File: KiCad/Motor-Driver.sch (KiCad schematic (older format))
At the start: 38 parts

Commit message: controller board schematic complete
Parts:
- gave numbers to parts that had none: 38

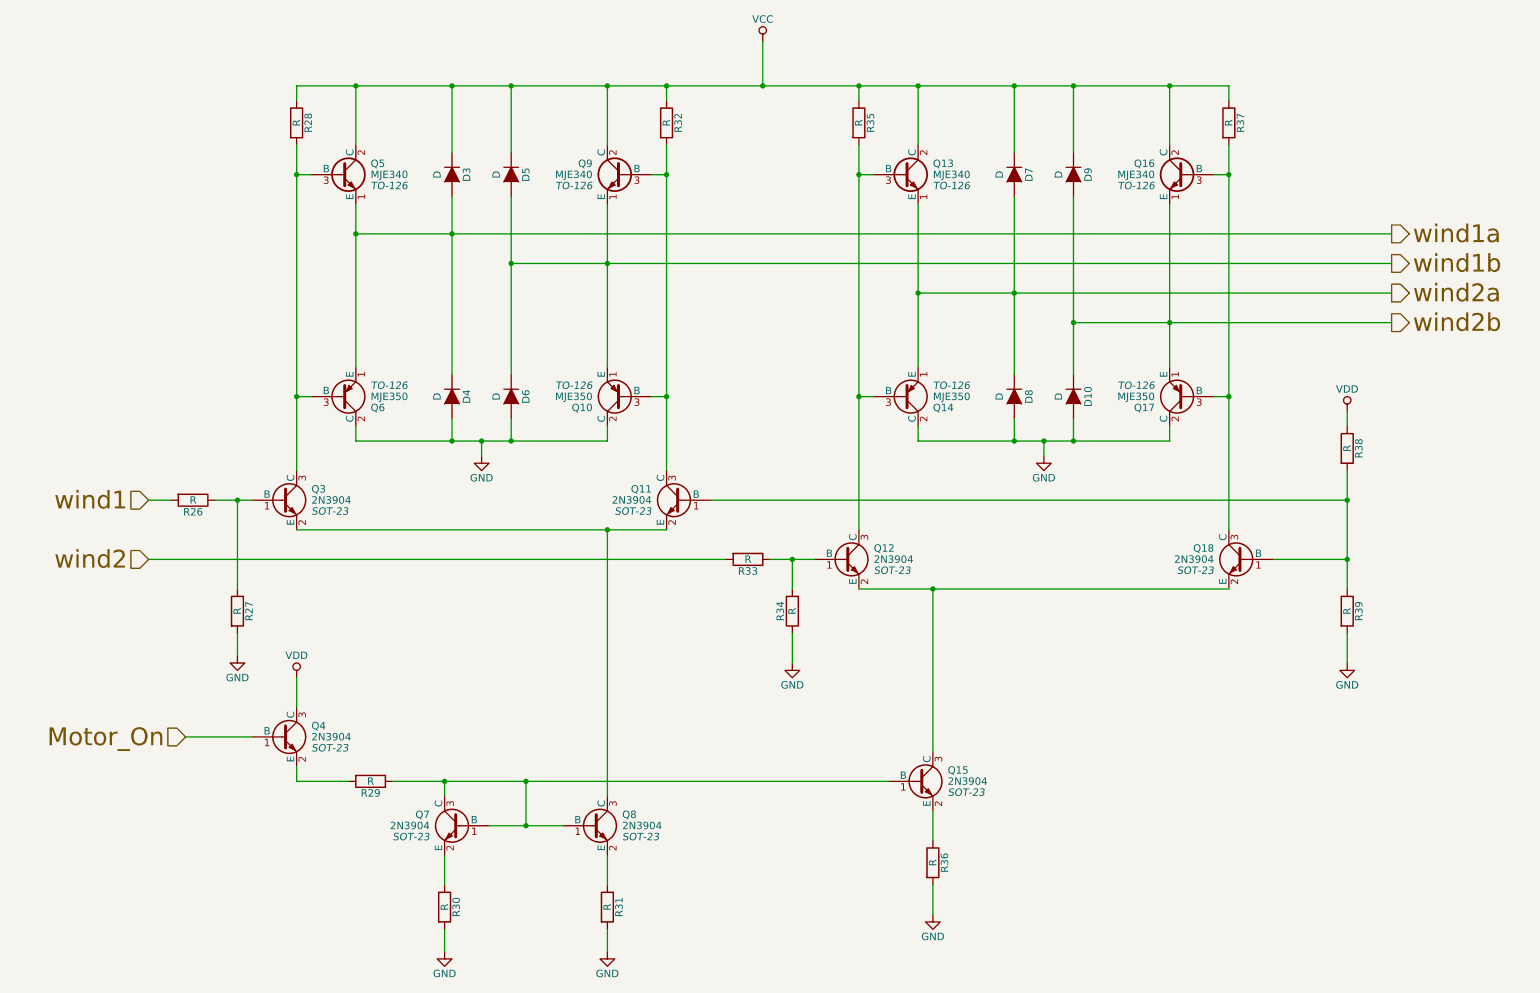
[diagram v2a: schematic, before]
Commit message: HeatOn fix, replaced R1-8 with array
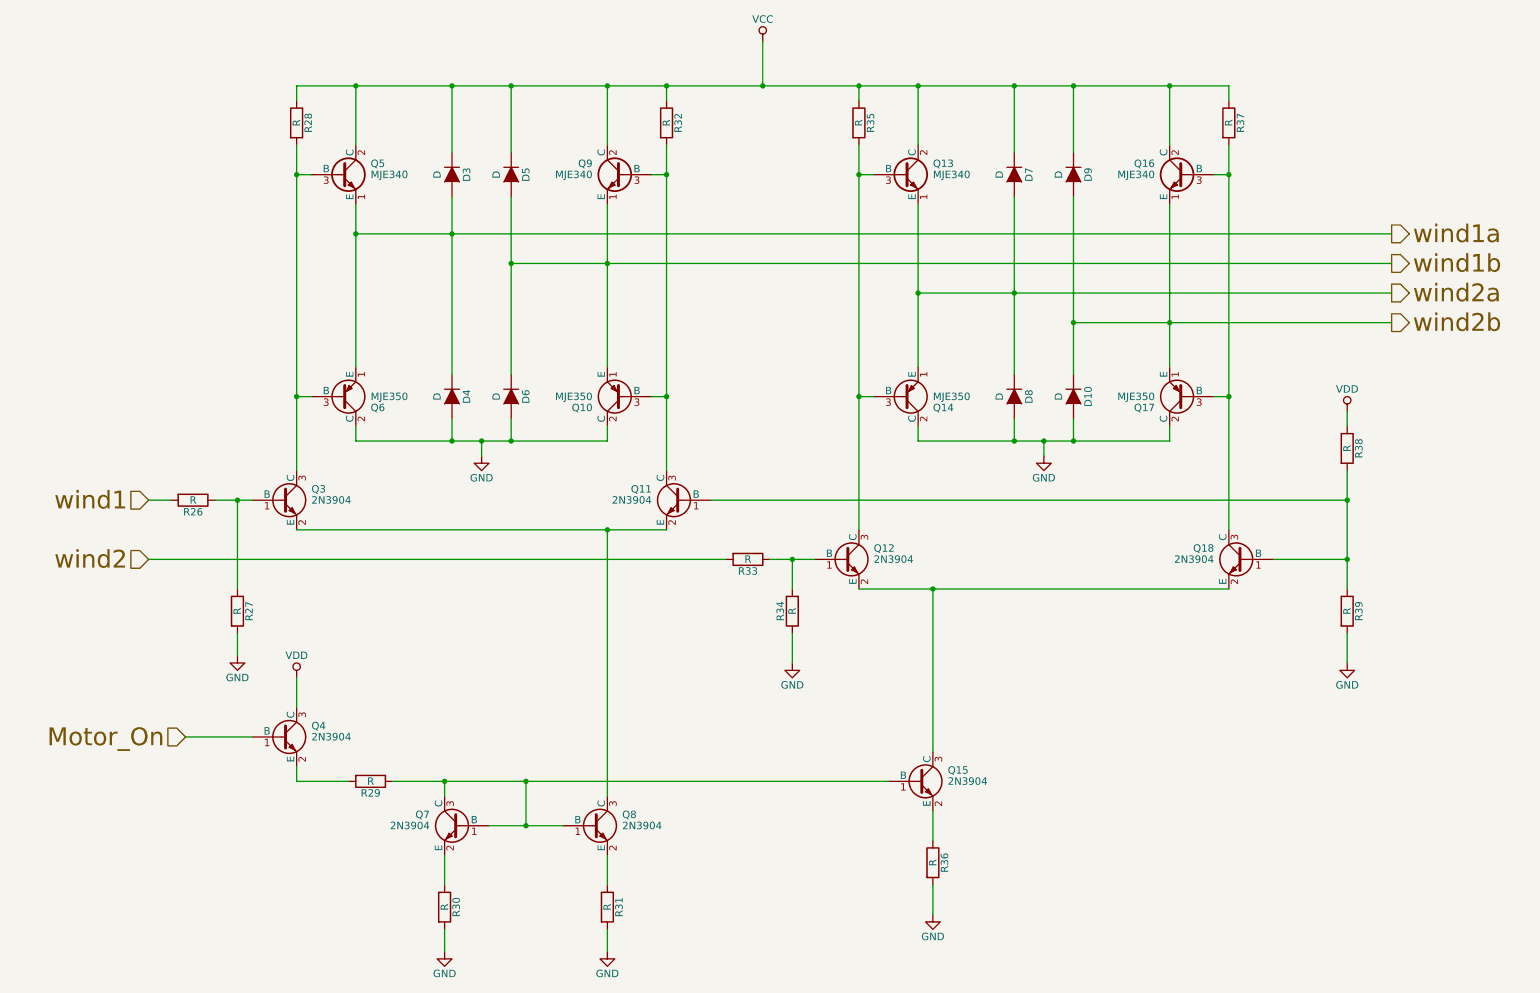
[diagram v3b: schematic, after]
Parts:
- Q10, Q13, Q14, Q16, Q17, Q5, Q6, Q9: footprint TO-126 -> (none)
- Q11, Q12, Q15, Q18, Q3, Q4, Q7, Q8: footprint SOT-23 -> (none)

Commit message: motor driver design
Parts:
- R26: value R -> 140
- R27: value R -> 115
- R28: renamed from R33; value R -> 140
- R29: renamed from R34; value R -> 115
- R30: renamed from R38; value R -> 64
- R31: renamed from R39; value R -> 64
- R32: renamed from R28; value R -> 165
- R33: renamed from R32; value R -> 165
- R34: renamed from R35; value R -> 165
- R35: renamed from R37; value R -> 165
- R36: renamed from R29; value R -> 51
- R37: renamed from R30; value R -> 10
- R38: renamed from R31; value R -> 10
- R39: renamed from R36; value R -> 10
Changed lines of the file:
@@
 $Descr A4 11693 8268
 encoding utf-8
-Sheet 4 6
+Sheet 5 6
 Title ""
 Date ""
@@
 $EndComp
 $Comp
-L R R28
+L R R32
 U 1 1 5681F689
 P 2300 1750
-F 0 "R28" V 2380 1750 50  0000 C CNN
-F 1 "R" V 2300 1750 50  0000 C CNN
+F 0 "R32" V 2380 1750 50  0000 C CNN
+F 1 "165" V 2300 1750 50  0000 C CNN
 F 2 "" V 2230 1750 50  0001 C CNN
 F 3 "" H 2300 1750 50  0000 C CNN
@@
 $EndComp
 $Comp
-L R R32
+L R R33
 U 1 1 5681F6D4
 P 4800 1750
-F 0 "R32" V 4880 1750 50  0000 C CNN
-F 1 "R" V 4800 1750 50  0000 C CNN
+F 0 "R33" V 4880 1750 50  0000 C CNN
+F 1 "165" V 4800 1750 50  0000 C CNN
 F 2 "" V 4730 1750 50  0001 C CNN
 F 3 "" H 4800 1750 50  0000 C CNN
@@
 $EndComp
 $Comp
-L R R35
+L R R34
 U 1 1 5681F715
 P 6100 1750
-F 0 "R35" V 6180 1750 50  0000 C CNN
-F 1 "R" V 6100 1750 50  0000 C CNN
+F 0 "R34" V 6180 1750 50  0000 C CNN
+F 1 "165" V 6100 1750 50  0000 C CNN
 F 2 "" V 6030 1750 50  0001 C CNN
 F 3 "" H 6100 1750 50  0000 C CNN
@@
 $EndComp
 $Comp
-L R R37
+L R R35
 U 1 1 5681F758
 P 8600 1750
-F 0 "R37" V 8680 1750 50  0000 C CNN
-F 1 "R" V 8600 1750 50  0000 C CNN
+F 0 "R35" V 8680 1750 50  0000 C CNN
+F 1 "165" V 8600 1750 50  0000 C CNN
 F 2 "" V 8530 1750 50  0001 C CNN
 F 3 "" H 8600 1750 50  0000 C CNN
@@
 $EndComp
 $Comp
-L R R38
+L R R30
 U 1 1 5681FC40
 P 9400 3950
-F 0 "R38" V 9480 3950 50  0000 C CNN
-F 1 "R" V 9400 3950 50  0000 C CNN
+F 0 "R30" V 9480 3950 50  0000 C CNN
+F 1 "64" V 9400 3950 50  0000 C CNN
 F 2 "" V 9330 3950 50  0001 C CNN
 F 3 "" H 9400 3950 50  0000 C CNN
@@
 $EndComp
 $Comp
-L R R39
+L R R31
 U 1 1 5681FD0B
 P 9400 5050
-F 0 "R39" V 9480 5050 50  0000 C CNN
-F 1 "R" V 9400 5050 50  0000 C CNN
+F 0 "R31" V 9480 5050 50  0000 C CNN
+F 1 "64" V 9400 5050 50  0000 C CNN
 F 2 "" V 9330 5050 50  0001 C CNN
 F 3 "" H 9400 5050 50  0000 C CNN
@@
 P 1600 4300
 F 0 "R26" V 1680 4300 50  0000 C CNN
-F 1 "R" V 1600 4300 50  0000 C CNN
+F 1 "140" V 1600 4300 50  0000 C CNN
 F 2 "" V 1530 4300 50  0001 C CNN
 F 3 "" H 1600 4300 50  0000 C CNN
@@
 $EndComp
 $Comp
-L R R33
+L R R28
 U 1 1 5681FF38
 P 5350 4700
-F 0 "R33" V 5430 4700 50  0000 C CNN
-F 1 "R" V 5350 4700 50  0000 C CNN
+F 0 "R28" V 5430 4700 50  0000 C CNN
+F 1 "140" V 5350 4700 50  0000 C CNN
 F 2 "" V 5280 4700 50  0001 C CNN
 F 3 "" H 5350 4700 50  0000 C CNN
@@
 $EndComp
 $Comp
-L R R34
+L R R29
 U 1 1 56820103
 P 5650 5050
-F 0 "R34" V 5730 5050 50  0000 C CNN
-F 1 "R" V 5650 5050 50  0000 C CNN
+F 0 "R29" V 5730 5050 50  0000 C CNN
+F 1 "115" V 5650 5050 50  0000 C CNN
 F 2 "" V 5580 5050 50  0001 C CNN
 F 3 "" H 5650 5050 50  0000 C CNN
@@
 P 1900 5050
 F 0 "R27" V 1980 5050 50  0000 C CNN
-F 1 "R" V 1900 5050 50  0000 C CNN
+F 1 "115" V 1900 5050 50  0000 C CNN
 F 2 "" V 1830 5050 50  0001 C CNN
 F 3 "" H 1900 5050 50  0000 C CNN
@@
 $EndComp
 $Comp
-L R R29
+L R R36
 U 1 1 568252C6
 P 2800 6200
-F 0 "R29" V 2880 6200 50  0000 C CNN
-F 1 "R" V 2800 6200 50  0000 C CNN
+F 0 "R36" V 2880 6200 50  0000 C CNN
+F 1 "51" V 2800 6200 50  0000 C CNN
 F 2 "" V 2730 6200 50  0001 C CNN
 F 3 "" H 2800 6200 50  0000 C CNN
@@
 	1550 5900 2000 5900
 $Comp
-L R R36
+L R R39
 U 1 1 56825779
 P 6600 6750
-F 0 "R36" V 6680 6750 50  0000 C CNN
-F 1 "R" V 6600 6750 50  0000 C CNN
+F 0 "R39" V 6680 6750 50  0000 C CNN
+F 1 "10" V 6600 6750 50  0000 C CNN
 F 2 "" V 6530 6750 50  0001 C CNN
 F 3 "" H 6600 6750 50  0000 C CNN
@@
 $EndComp
 $Comp
-L R R31
+L R R38
 U 1 1 568257DC
 P 4400 7050
-F 0 "R31" V 4480 7050 50  0000 C CNN
-F 1 "R" V 4400 7050 50  0000 C CNN
+F 0 "R38" V 4480 7050 50  0000 C CNN
+F 1 "10" V 4400 7050 50  0000 C CNN
 F 2 "" V 4330 7050 50  0001 C CNN
 F 3 "" H 4400 7050 50  0000 C CNN
@@
 $EndComp
 $Comp
-L R R30
+L R R37
 U 1 1 568258D1
 P 3300 7050
-F 0 "R30" V 3380 7050 50  0000 C CNN
-F 1 "R" V 3300 7050 50  0000 C CNN
+F 0 "R37" V 3380 7050 50  0000 C CNN
+F 1 "10" V 3300 7050 50  0000 C CNN
 F 2 "" V 3230 7050 50  0001 C CNN
 F 3 "" H 3300 7050 50  0000 C CNN

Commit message: kicad resistor package associations complete
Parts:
- R26, R27, R28, R29, R30, R31, R36, R37, R38, R39: footprint (none) -> Resistors_ThroughHole:Resistor_Horizontal_RM10mm
- R32, R33, R34, R35: footprint (none) -> Resistors_ThroughHole:Resistor_Horizontal_RM15mm
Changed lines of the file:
@@
 F 0 "R32" V 2380 1750 50  0000 C CNN
 F 1 "165" V 2300 1750 50  0000 C CNN
-F 2 "" V 2230 1750 50  0001 C CNN
+F 2 "Resistors_ThroughHole:Resistor_Horizontal_RM15mm" V 2230 1750 50  0001 C CNN
 F 3 "" H 2300 1750 50  0000 C CNN
 	1    2300 1750
@@
 F 0 "R33" V 4880 1750 50  0000 C CNN
 F 1 "165" V 4800 1750 50  0000 C CNN
-F 2 "" V 4730 1750 50  0001 C CNN
+F 2 "Resistors_ThroughHole:Resistor_Horizontal_RM15mm" V 4730 1750 50  0001 C CNN
 F 3 "" H 4800 1750 50  0000 C CNN
 	1    4800 1750
@@
 F 0 "R34" V 6180 1750 50  0000 C CNN
 F 1 "165" V 6100 1750 50  0000 C CNN
-F 2 "" V 6030 1750 50  0001 C CNN
+F 2 "Resistors_ThroughHole:Resistor_Horizontal_RM15mm" V 6030 1750 50  0001 C CNN
 F 3 "" H 6100 1750 50  0000 C CNN
 	1    6100 1750
@@
 F 0 "R35" V 8680 1750 50  0000 C CNN
 F 1 "165" V 8600 1750 50  0000 C CNN
-F 2 "" V 8530 1750 50  0001 C CNN
+F 2 "Resistors_ThroughHole:Resistor_Horizontal_RM15mm" V 8530 1750 50  0001 C CNN
 F 3 "" H 8600 1750 50  0000 C CNN
 	1    8600 1750
@@
 F 0 "R30" V 9480 3950 50  0000 C CNN
 F 1 "64" V 9400 3950 50  0000 C CNN
-F 2 "" V 9330 3950 50  0001 C CNN
+F 2 "Resistors_ThroughHole:Resistor_Horizontal_RM10mm" V 9330 3950 50  0001 C CNN
 F 3 "" H 9400 3950 50  0000 C CNN
 	1    9400 3950
@@
 F 0 "R31" V 9480 5050 50  0000 C CNN
 F 1 "64" V 9400 5050 50  0000 C CNN
-F 2 "" V 9330 5050 50  0001 C CNN
+F 2 "Resistors_ThroughHole:Resistor_Horizontal_RM10mm" V 9330 5050 50  0001 C CNN
 F 3 "" H 9400 5050 50  0000 C CNN
 	1    9400 5050
@@
 F 0 "R26" V 1680 4300 50  0000 C CNN
 F 1 "140" V 1600 4300 50  0000 C CNN
-F 2 "" V 1530 4300 50  0001 C CNN
+F 2 "Resistors_ThroughHole:Resistor_Horizontal_RM10mm" V 1530 4300 50  0001 C CNN
 F 3 "" H 1600 4300 50  0000 C CNN
 	1    1600 4300
@@
 F 0 "R28" V 5430 4700 50  0000 C CNN
 F 1 "140" V 5350 4700 50  0000 C CNN
-F 2 "" V 5280 4700 50  0001 C CNN
+F 2 "Resistors_ThroughHole:Resistor_Horizontal_RM10mm" V 5280 4700 50  0001 C CNN
 F 3 "" H 5350 4700 50  0000 C CNN
 	1    5350 4700
@@
 F 0 "R29" V 5730 5050 50  0000 C CNN
 F 1 "115" V 5650 5050 50  0000 C CNN
-F 2 "" V 5580 5050 50  0001 C CNN
+F 2 "Resistors_ThroughHole:Resistor_Horizontal_RM10mm" V 5580 5050 50  0001 C CNN
 F 3 "" H 5650 5050 50  0000 C CNN
 	1    5650 5050
@@
 F 0 "R27" V 1980 5050 50  0000 C CNN
 F 1 "115" V 1900 5050 50  0000 C CNN
-F 2 "" V 1830 5050 50  0001 C CNN
+F 2 "Resistors_ThroughHole:Resistor_Horizontal_RM10mm" V 1830 5050 50  0001 C CNN
 F 3 "" H 1900 5050 50  0000 C CNN
 	1    1900 5050
@@
 F 0 "R36" V 2880 6200 50  0000 C CNN
 F 1 "51" V 2800 6200 50  0000 C CNN
-F 2 "" V 2730 6200 50  0001 C CNN
+F 2 "Resistors_ThroughHole:Resistor_Horizontal_RM10mm" V 2730 6200 50  0001 C CNN
 F 3 "" H 2800 6200 50  0000 C CNN
 	1    2800 6200
@@
 F 0 "R39" V 6680 6750 50  0000 C CNN
 F 1 "10" V 6600 6750 50  0000 C CNN
-F 2 "" V 6530 6750 50  0001 C CNN
+F 2 "Resistors_ThroughHole:Resistor_Horizontal_RM10mm" V 6530 6750 50  0001 C CNN
 F 3 "" H 6600 6750 50  0000 C CNN
 	1    6600 6750
@@
 F 0 "R38" V 4480 7050 50  0000 C CNN
 F 1 "10" V 4400 7050 50  0000 C CNN
-F 2 "" V 4330 7050 50  0001 C CNN
+F 2 "Resistors_ThroughHole:Resistor_Horizontal_RM10mm" V 4330 7050 50  0001 C CNN
 F 3 "" H 4400 7050 50  0000 C CNN
 	1    4400 7050
@@
 F 0 "R37" V 3380 7050 50  0000 C CNN
 F 1 "10" V 3300 7050 50  0000 C CNN
-F 2 "" V 3230 7050 50  0001 C CNN
+F 2 "Resistors_ThroughHole:Resistor_Horizontal_RM10mm" V 3230 7050 50  0001 C CNN
 F 3 "" H 3300 7050 50  0000 C CNN
 	1    3300 7050

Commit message: capacitors and diode part associations
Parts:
- D10, D3, D4, D5, D6, D7, D8, D9: footprint (none) -> Discret:D3
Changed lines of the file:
@@
 F 0 "D3" H 3350 2200 50  0000 C CNN
 F 1 "D" H 3350 2000 50  0000 C CNN
-F 2 "" H 3350 2100 50  0001 C CNN
+F 2 "Discret:D3" H 3350 2100 50  0001 C CNN
 F 3 "" H 3350 2100 50  0000 C CNN
 	1    3350 2100
@@
 F 0 "D4" H 3350 3700 50  0000 C CNN
 F 1 "D" H 3350 3500 50  0000 C CNN
-F 2 "" H 3350 3600 50  0001 C CNN
+F 2 "Discret:D3" H 3350 3600 50  0001 C CNN
 F 3 "" H 3350 3600 50  0000 C CNN
 	1    3350 3600
@@
 F 0 "D5" H 3750 2200 50  0000 C CNN
 F 1 "D" H 3750 2000 50  0000 C CNN
-F 2 "" H 3750 2100 50  0001 C CNN
+F 2 "Discret:D3" H 3750 2100 50  0001 C CNN
 F 3 "" H 3750 2100 50  0000 C CNN
 	1    3750 2100
@@
 F 0 "D6" H 3750 3700 50  0000 C CNN
 F 1 "D" H 3750 3500 50  0000 C CNN
-F 2 "" H 3750 3600 50  0001 C CNN
+F 2 "Discret:D3" H 3750 3600 50  0001 C CNN
 F 3 "" H 3750 3600 50  0000 C CNN
 	1    3750 3600
@@
 F 0 "D7" H 7150 2200 50  0000 C CNN
 F 1 "D" H 7150 2000 50  0000 C CNN
-F 2 "" H 7150 2100 50  0001 C CNN
+F 2 "Discret:D3" H 7150 2100 50  0001 C CNN
 F 3 "" H 7150 2100 50  0000 C CNN
 	1    7150 2100
@@
 F 0 "D8" H 7150 3700 50  0000 C CNN
 F 1 "D" H 7150 3500 50  0000 C CNN
-F 2 "" H 7150 3600 50  0001 C CNN
+F 2 "Discret:D3" H 7150 3600 50  0001 C CNN
 F 3 "" H 7150 3600 50  0000 C CNN
 	1    7150 3600
@@
 F 0 "D9" H 7550 2200 50  0000 C CNN
 F 1 "D" H 7550 2000 50  0000 C CNN
-F 2 "" H 7550 2100 50  0001 C CNN
+F 2 "Discret:D3" H 7550 2100 50  0001 C CNN
 F 3 "" H 7550 2100 50  0000 C CNN
 	1    7550 2100
@@
 F 0 "D10" H 7550 3700 50  0000 C CNN
 F 1 "D" H 7550 3500 50  0000 C CNN
-F 2 "" H 7550 3600 50  0001 C CNN
+F 2 "Discret:D3" H 7550 3600 50  0001 C CNN
 F 3 "" H 7550 3600 50  0000 C CNN
 	1    7550 3600

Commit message: IC BOM and footprints complete
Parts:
- removed Q11, Q12, Q15, Q18, Q3, Q4, Q7, Q8: 2N3904, symbol MMBT3904
- added Q11, Q12, Q15, Q18, Q3, Q4, Q7, Q8: 2N3904, Easy-PCB-footprints:TO-92, symbol 2N3904
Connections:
- net Motor_On: now also Q4.2 (B)
- net VDD: now also Q4.3 (C)
- net at Q10.3 (B), Q9.3 (B), R33.2: now also Q11.3 (C)
- net at Q13.3 (B), Q14.3 (B), R34.2: now also Q12.3 (C)
- net at Q16.3 (B), Q17.3 (B), R35.2: now also Q18.3 (C)
- net at Q5.3 (B), Q6.3 (B), R32.2: now also Q3.3 (C)
- net at R30.2, R31.1: now also Q11.2 (B), Q18.2 (B)
- net at R28.1, R29.2: now also Q12.2 (B)
- net at R26.1, R27.1: now also Q3.2 (B)
- net at R36.2: now also Q4.1 (E)
- net at R36.1: now also Q15.2 (B), Q7.2 (B), Q7.3 (C), Q8.2 (B)
- net at R37.1: now also Q7.1 (E)
- net at R38.1: now also Q8.1 (E)
- net at R39.1: now also Q15.1 (E)
- new net: Q11.1 (E), Q3.1 (E), Q8.3 (C)
- new net: Q12.1 (E), Q15.3 (C), Q18.1 (E)
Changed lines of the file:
@@
-$EndComp
-$Comp
-L MMBT3904 Q11
-U 1 1 5681EB1C
-P 4900 4300
-F 0 "Q11" H 5100 4375 50  0000 L CNN
-F 1 "2N3904" H 5100 4300 50  0000 L CNN
-F 2 "" H 5100 4225 50  0001 L CIN
-F 3 "" H 4900 4300 50  0000 L CNN
-	1    4900 4300
-	-1   0    0    -1
-$EndComp
-$Comp
-L MMBT3904 Q12
-U 1 1 5681EDF8
-P 6000 4700
-F 0 "Q12" H 6200 4775 50  0000 L CNN
-F 1 "2N3904" H 6200 4700 50  0000 L CNN
-F 2 "" H 6200 4625 50  0001 L CIN
-F 3 "" H 6000 4700 50  0000 L CNN
-	1    6000 4700
-	1    0    0    -1
-$EndComp
-$Comp
-L MMBT3904 Q18
-U 1 1 5681F30D
-P 8700 4700
-F 0 "Q18" H 8900 4775 50  0000 L CNN
-F 1 "2N3904" H 8900 4700 50  0000 L CNN
-F 2 "" H 8900 4625 50  0001 L CIN
-F 3 "" H 8700 4700 50  0000 L CNN
-	1    8700 4700
-	-1   0    0    -1
-$EndComp
-$Comp
-L MMBT3904 Q3
-U 1 1 5681F3C0
-P 2200 4300
-F 0 "Q3" H 2400 4375 50  0000 L CNN
-F 1 "2N3904" H 2400 4300 50  0000 L CNN
-F 2 "" H 2400 4225 50  0001 L CIN
-F 3 "" H 2200 4300 50  0000 L CNN
-	1    2200 4300
-	1    0    0    -1
 $EndComp
 $Comp
@@
 Motor_On
 $Comp
-L MMBT3904 Q4
-U 1 1 56823A81
-P 2200 5900
-F 0 "Q4" H 2400 5975 50  0000 L CNN
-F 1 "2N3904" H 2400 5900 50  0000 L CNN
-F 2 "" H 2400 5825 50  0001 L CIN
-F 3 "" H 2200 5900 50  0000 L CNN
-	1    2200 5900
-	1    0    0    -1
-$EndComp
-$Comp
-L MMBT3904 Q7
-U 1 1 56823DB9
-P 3400 6500
-F 0 "Q7" H 3600 6575 50  0000 L CNN
-F 1 "2N3904" H 3600 6500 50  0000 L CNN
-F 2 "" H 3600 6425 50  0001 L CIN
-F 3 "" H 3400 6500 50  0000 L CNN
-	1    3400 6500
-	-1   0    0    -1
-$EndComp
-$Comp
-L MMBT3904 Q8
-U 1 1 56823E0E
-P 4300 6500
-F 0 "Q8" H 4500 6575 50  0000 L CNN
-F 1 "2N3904" H 4500 6500 50  0000 L CNN
-F 2 "" H 4500 6425 50  0001 L CIN
-F 3 "" H 4300 6500 50  0000 L CNN
-	1    4300 6500
-	1    0    0    -1
-$EndComp
-$Comp
-L MMBT3904 Q15
-U 1 1 56823E6F
-P 6500 6200
-F 0 "Q15" H 6700 6275 50  0000 L CNN
-F 1 "2N3904" H 6700 6200 50  0000 L CNN
-F 2 "" H 6700 6125 50  0001 L CIN
-F 3 "" H 6500 6200 50  0000 L CNN
-	1    6500 6200
-	1    0    0    -1
-$EndComp
-$Comp
 L R R36
 U 1 1 568252C6
@@
 Wire Wire Line
 	6600 6900 6600 7100
+$Comp
+L 2N3904 Q3
+U 1 1 568814C5
+P 2200 4300
+F 0 "Q3" H 2400 4375 50  0000 L CNN
+F 1 "2N3904" H 2400 4300 50  0000 L CNN
+F 2 "Easy-PCB-footprints:TO-92" H 2400 4225 50  0000 L CIN
+F 3 "" H 2200 4300 50  0000 L CNN
+	1    2200 4300
+	1    0    0    -1
+$EndComp
+$Comp
+L 2N3904 Q11
+U 1 1 56881680
+P 4900 4300
+F 0 "Q11" H 5100 4375 50  0000 L CNN
+F 1 "2N3904" H 5100 4300 50  0000 L CNN
+F 2 "Easy-PCB-footprints:TO-92" H 5100 4225 50  0000 L CIN
+F 3 "" H 4900 4300 50  0000 L CNN
+	1    4900 4300
+	-1   0    0    -1
+$EndComp
+$Comp
+L 2N3904 Q12
+U 1 1 56881817
+P 6000 4700
+F 0 "Q12" H 6200 4775 50  0000 L CNN
+F 1 "2N3904" H 6200 4700 50  0000 L CNN
+F 2 "Easy-PCB-footprints:TO-92" H 6200 4625 50  0000 L CIN
+F 3 "" H 6000 4700 50  0000 L CNN
+	1    6000 4700
+	1    0    0    -1
+$EndComp
+$Comp
+L 2N3904 Q18
+U 1 1 56881960
+P 8700 4700
+F 0 "Q18" H 8900 4775 50  0000 L CNN
+F 1 "2N3904" H 8900 4700 50  0000 L CNN
+F 2 "Easy-PCB-footprints:TO-92" H 8900 4625 50  0000 L CIN
+F 3 "" H 8700 4700 50  0000 L CNN
+	1    8700 4700
+	-1   0    0    -1
+$EndComp
+$Comp
+L 2N3904 Q15
+U 1 1 56881BB3
+P 6500 6200
+F 0 "Q15" H 6700 6275 50  0000 L CNN
+F 1 "2N3904" H 6700 6200 50  0000 L CNN
+F 2 "Easy-PCB-footprints:TO-92" H 6700 6125 50  0000 L CIN
+F 3 "" H 6500 6200 50  0000 L CNN
+	1    6500 6200
+	1    0    0    -1
+$EndComp
+$Comp
+L 2N3904 Q8
+U 1 1 56881E2C
+P 4300 6500
+F 0 "Q8" H 4500 6575 50  0000 L CNN
+F 1 "2N3904" H 4500 6500 50  0000 L CNN
+F 2 "Easy-PCB-footprints:TO-92" H 4500 6425 50  0000 L CIN
+F 3 "" H 4300 6500 50  0000 L CNN
+	1    4300 6500
+	1    0    0    -1
+$EndComp
+$Comp
+L 2N3904 Q7
+U 1 1 56881FE9
+P 3400 6500
+F 0 "Q7" H 3600 6575 50  0000 L CNN
+F 1 "2N3904" H 3600 6500 50  0000 L CNN
+F 2 "Easy-PCB-footprints:TO-92" H 3600 6425 50  0000 L CIN
+F 3 "" H 3400 6500 50  0000 L CNN
+	1    3400 6500
+	-1   0    0    -1
+$EndComp
+$Comp
+L 2N3904 Q4
+U 1 1 5688217E
+P 2200 5900
+F 0 "Q4" H 2400 5975 50  0000 L CNN
+F 1 "2N3904" H 2400 5900 50  0000 L CNN
+F 2 "Easy-PCB-footprints:TO-92" H 2400 5825 50  0000 L CIN
+F 3 "" H 2200 5900 50  0000 L CNN
+	1    2200 5900
+	1    0    0    -1
+$EndComp
 $EndSCHEMATC
